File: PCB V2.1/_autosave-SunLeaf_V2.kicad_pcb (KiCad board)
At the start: 4 copper layers, 77 x 40 mm, 111 parts, among them IC1 ESP_09, J1 20021121-00010C4LF, J10 B4B-PH-K-S(LF)(SN), J11 B4B-PH-K-S(LF)(SN), J12 B4B-PH-K-S(LF)(SN), J13 B4B-PH-K-S(LF)(SN), J14 B4B-PH-K-S(LF)(SN), J15 B4B-PH-K-S(LF)(SN), J16 B4B-PH-K-S(LF)(SN), J2 0475890001-MicroUSBPort, J3 B2B-PH-K-S(LF)(SN), J4 B3B-PH-K-S(LF)(SN), J5 B4B-PH-K-S(LF)(SN), J6 B4B-PH-K-S(LF)(SN), J7 B4B-PH-K-S(LF)(SN), J8 B4B-PH-K-S(LF)(SN), J9 B4B-PH-K-S(LF)(SN), P1 CONN_01X04, Q1 DMG2307L-7, Q2 DMG2307L-7, SW1 B3U-1000P, SW2 B3U-1000P, T1 1909763-1, U1 STM32F446RET6_-_TQFP64, U2 BQ24210DQCT, U3 AZ1117CR-3.3TRG1_1, U4 74HC4052D, U5 PCA9518DBQR, X1 ABM3B8.000MHZB2T, X2 ABS07-32.768KHZ-9-T

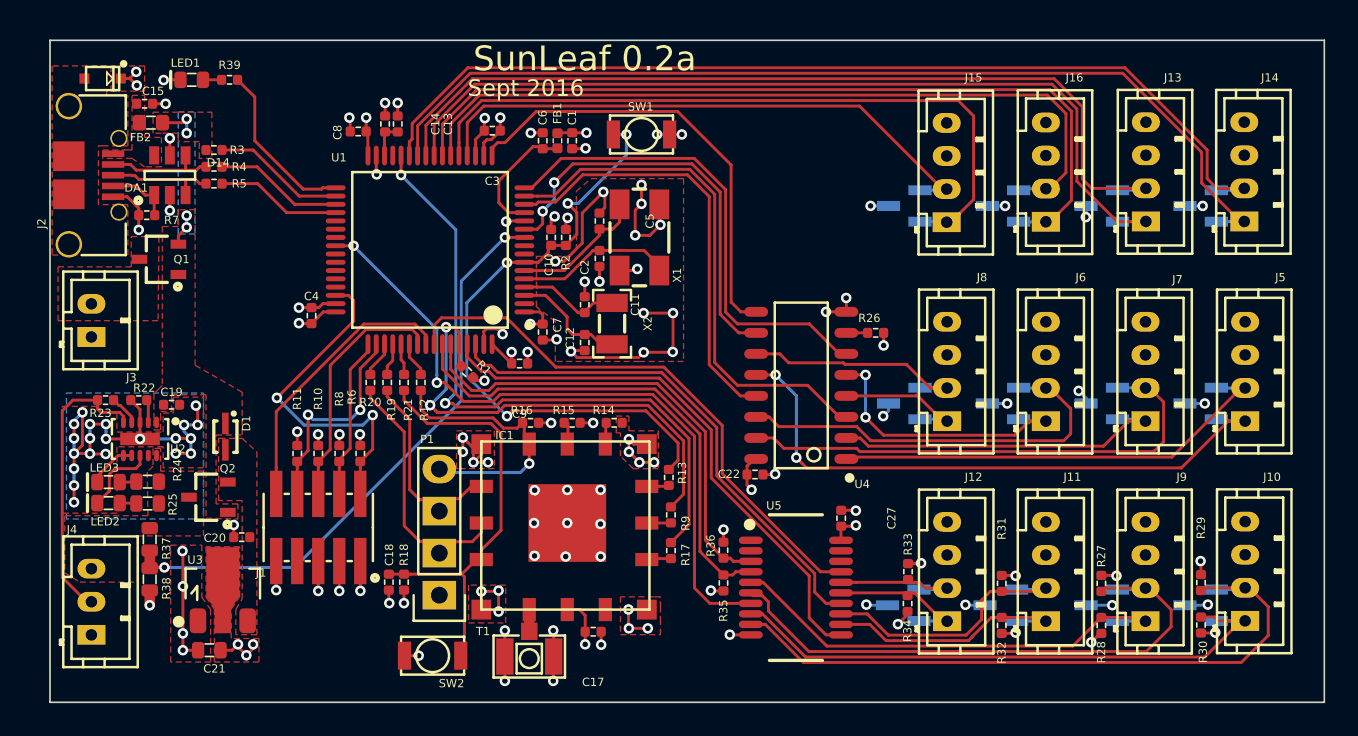
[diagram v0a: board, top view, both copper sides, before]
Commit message: Battery Monitoring & OTA
OTA signals between both processors solidified and routed. Battery
monitoring added as voltage divider into ADC channel. All but done
pending some small tweaks.
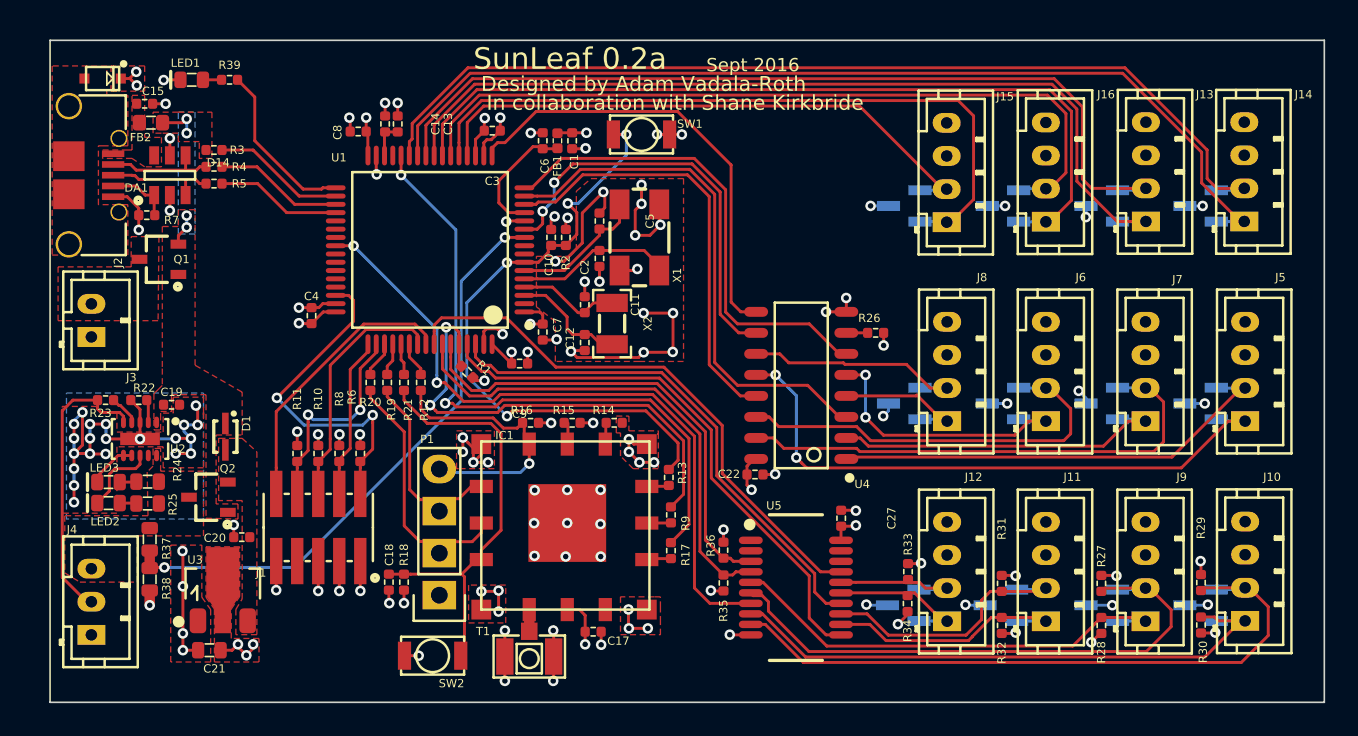
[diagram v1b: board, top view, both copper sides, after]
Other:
- board text added: "Designed by Adam Vadala-Roth"
- board text added: "In collaboration with Shane Kirkbride"
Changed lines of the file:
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@@
     (area 42.949999 29.949999 120.050001 70.050001)
     (thickness 1.6)
-    (drawings 16)
+    (drawings 18)
     (tracks 1126)
     (zones 0)
@@
     (descr http://www.jst-mfg.com/product/pdf/eng/ePH.pdf)
     (tags "connector jst ph")
-    (fp_text reference J16 (at 8.7056 1.7272 180) (layer F.SilkS)
+    (fp_text reference J16 (at 7.6896 3.6322 180) (layer F.SilkS)
       (effects (font (size 0.5 0.5) (thickness 0.1)))
     )
@@
     (descr http://www.jst-mfg.com/product/pdf/eng/ePH.pdf)
     (tags "connector jst ph")
-    (fp_text reference J13 (at 8.6868 1.6256) (layer F.SilkS)
+    (fp_text reference J13 (at 7.6708 3.556) (layer F.SilkS)
       (effects (font (size 0.5 0.5) (thickness 0.1)))
     )
@@
     (descr http://www.jst-mfg.com/product/pdf/eng/ePH.pdf)
     (tags "connector jst ph")
-    (fp_text reference J15 (at 8.731 1.6256 180) (layer F.SilkS)
+    (fp_text reference J15 (at 7.588 3.5306 180) (layer F.SilkS)
       (effects (font (size 0.5 0.5) (thickness 0.1)))
     )
@@
     (descr http://www.jst-mfg.com/product/pdf/eng/ePH.pdf)
     (tags "connector jst ph")
-    (fp_text reference J14 (at 8.6868 1.5494) (layer F.SilkS)
+    (fp_text reference J14 (at 7.6708 3.5814) (layer F.SilkS)
       (effects (font (size 0.5 0.5) (thickness 0.1)))
     )
@@
   (module PCB_Footprints:C0402 (layer F.Cu)
     (at 72.771 36.068 90)
-    (fp_text reference C6 (at 1.397 0 90) (layer F.SilkS)
+    (fp_text reference C6 (at -1.524 0.127 90) (layer F.SilkS)
       (effects (font (size 0.5 0.5) (thickness 0.1)))
     )
@@
   (module PCB_Footprints:B3U-1000P (layer F.Cu)
     (at 78.74 35.687)
-    (fp_text reference SW1 (at -0.0508 -1.6764) (layer F.SilkS)
+    (fp_text reference SW1 (at 2.921 -0.635) (layer F.SilkS)
       (effects (font (size 0.5 0.5) (thickness 0.1)))
     )
@@
   (module PCB_Footprints:C0402 (layer F.Cu)
     (at 74.549 36.068 270)
-    (fp_text reference C1 (at -1.397 0 270) (layer F.SilkS)
+    (fp_text reference C1 (at 1.27 -0.127 270) (layer F.SilkS)
       (effects (font (size 0.5 0.5) (thickness 0.1)))
     )
@@
   (module PCB_Footprints:BLM15HG601SN1D (layer F.Cu)
     (at 73.66 36.068 270)
-    (fp_text reference FB1 (at -1.651 0 270) (layer F.SilkS)
+    (fp_text reference FB1 (at 1.524 0 270) (layer F.SilkS)
       (effects (font (size 0.5 0.5) (thickness 0.1)))
     )
@@
   (module PCB_Footprints:C0402 (layer F.Cu)
     (at 75.819 65.7352)
-    (fp_text reference C17 (at 0 3.048) (layer F.SilkS)
+    (fp_text reference C17 (at 1.524 0.5588) (layer F.SilkS)
       (effects (font (size 0.5 0.5) (thickness 0.1)))
     )
@@
   (module PCB_Footprints:0475890001 (layer F.Cu)
     (at 46.8122 38.1508 90)
-    (fp_text reference J2 (at -2.921 -4.318 90) (layer F.SilkS)
+    (fp_text reference J2 (at -5.2832 0.3048 90) (layer F.SilkS)
       (effects (font (size 0.5 0.5) (thickness 0.1)))
     )
@@
       (net 2 GND))
   )
-  (gr_text "Sept 2016" (at 71.755 32.893) (layer F.SilkS)
-    (effects (font (size 1 1) (thickness 0.17)))
+  (gr_text "In collaboration with Shane Kirkbride" (at 80.772 33.782) (layer F.SilkS)
+    (effects (font (size 0.9 0.9) (thickness 0.17)))
   )
-  (gr_text "SunLeaf 0.2a" (at 75.311 31.115) (layer F.SilkS)
-    (effects (font (size 1.5 1.5) (thickness 0.3)))
+  (gr_text "Designed by Adam Vadala-Roth\n" (at 78.867 32.639) (layer F.SilkS)
+    (effects (font (size 0.9 0.9) (thickness 0.17)))
+  )
+  (gr_text "Sept 2016" (at 85.471 31.496) (layer F.SilkS)
+    (effects (font (size 0.8 0.8) (thickness 0.17)))
+  )
+  (gr_text "SunLeaf 0.2a" (at 74.422 31.115) (layer F.SilkS)
+    (effects (font (size 1.3 1.3) (thickness 0.3)))
   )
   (gr_line (start 100 30) (end 100 70) (layer F.CrtYd) (width 0.1))
